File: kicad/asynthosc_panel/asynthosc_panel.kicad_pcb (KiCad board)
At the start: 2 copper layers, 71.1 x 128.4 mm, 0 parts

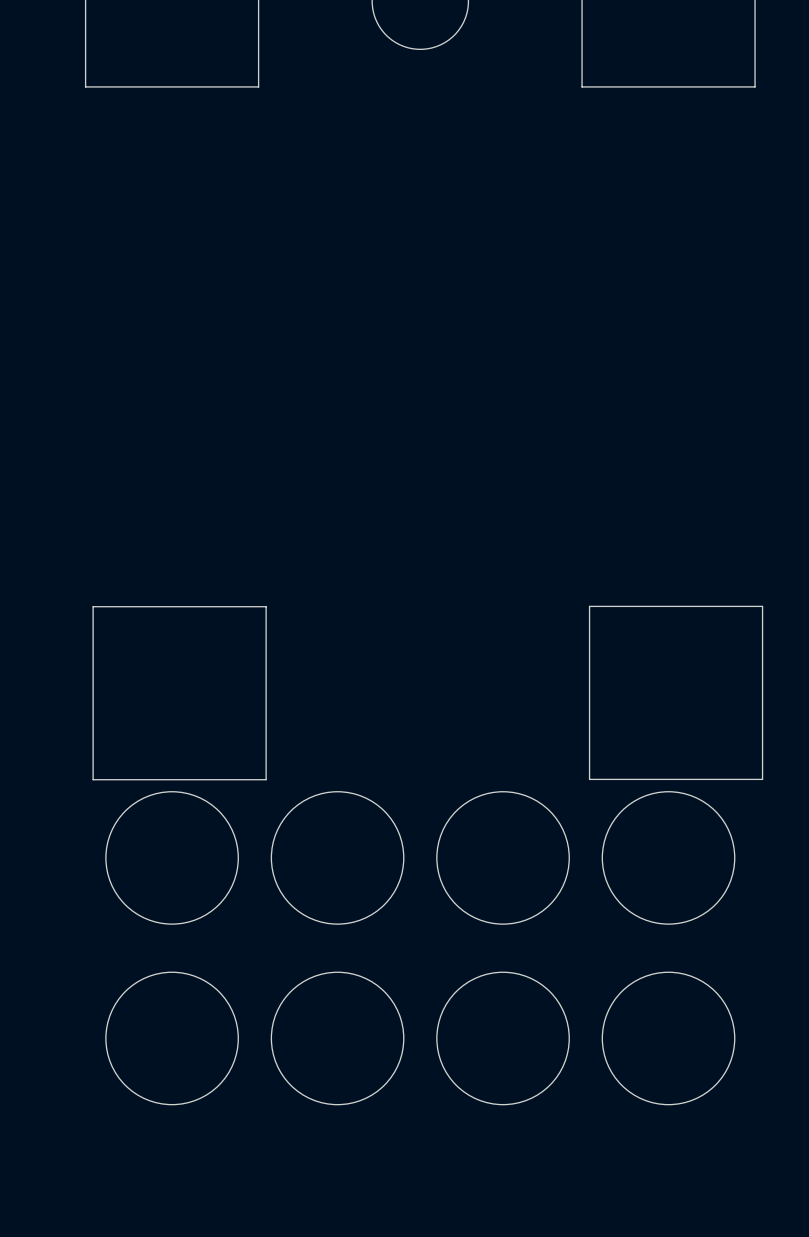
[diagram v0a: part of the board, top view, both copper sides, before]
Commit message: [MECA] Add 1mm milling contour
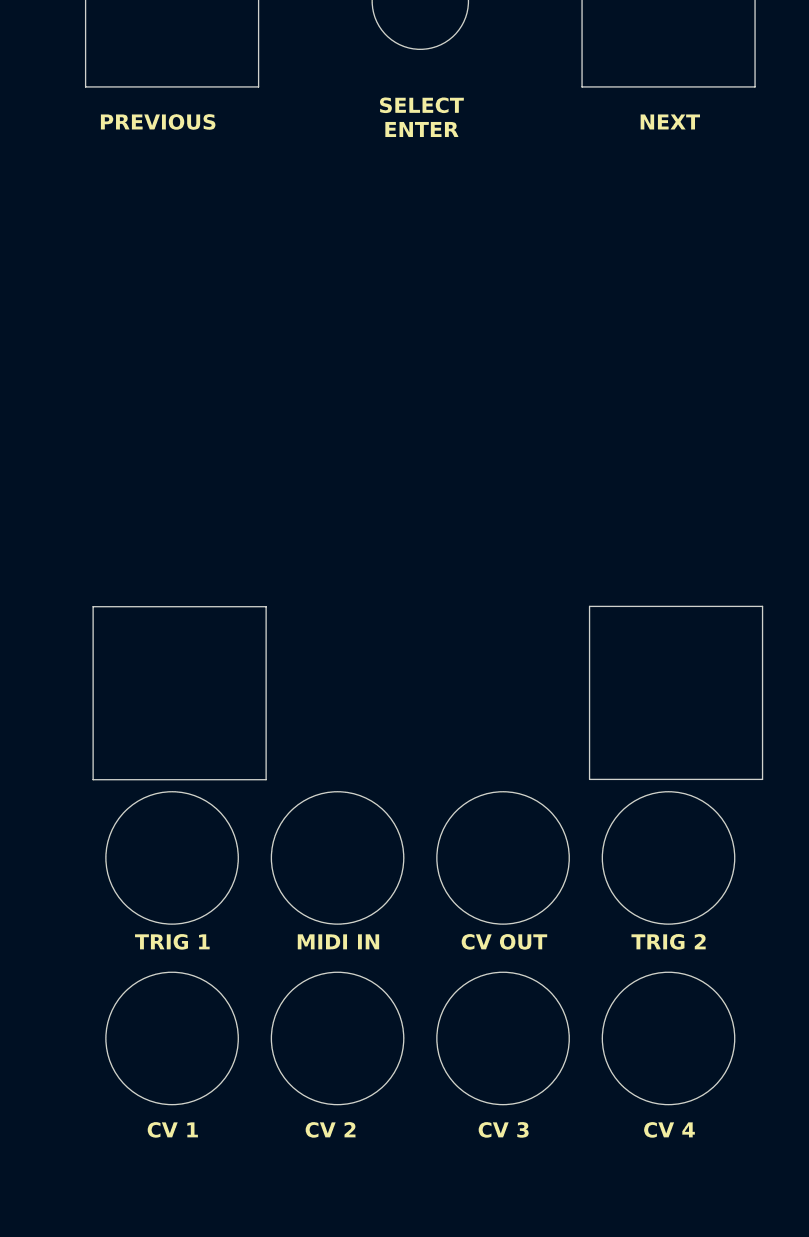
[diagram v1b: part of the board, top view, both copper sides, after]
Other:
- board text added: "CV 1"
- board text added: "CV 2"
- board text added: "CV 3"
- board text added: "CV 4"
- board text added: "CV OUT"
- board text added: "MIDI IN"
- board text added: "NEXT"
- board text added: "PREVIOUS"
- board text added: "SELECT ENTER"
- board text added: "TRIG 1"
- board text added: "TRIG 2"

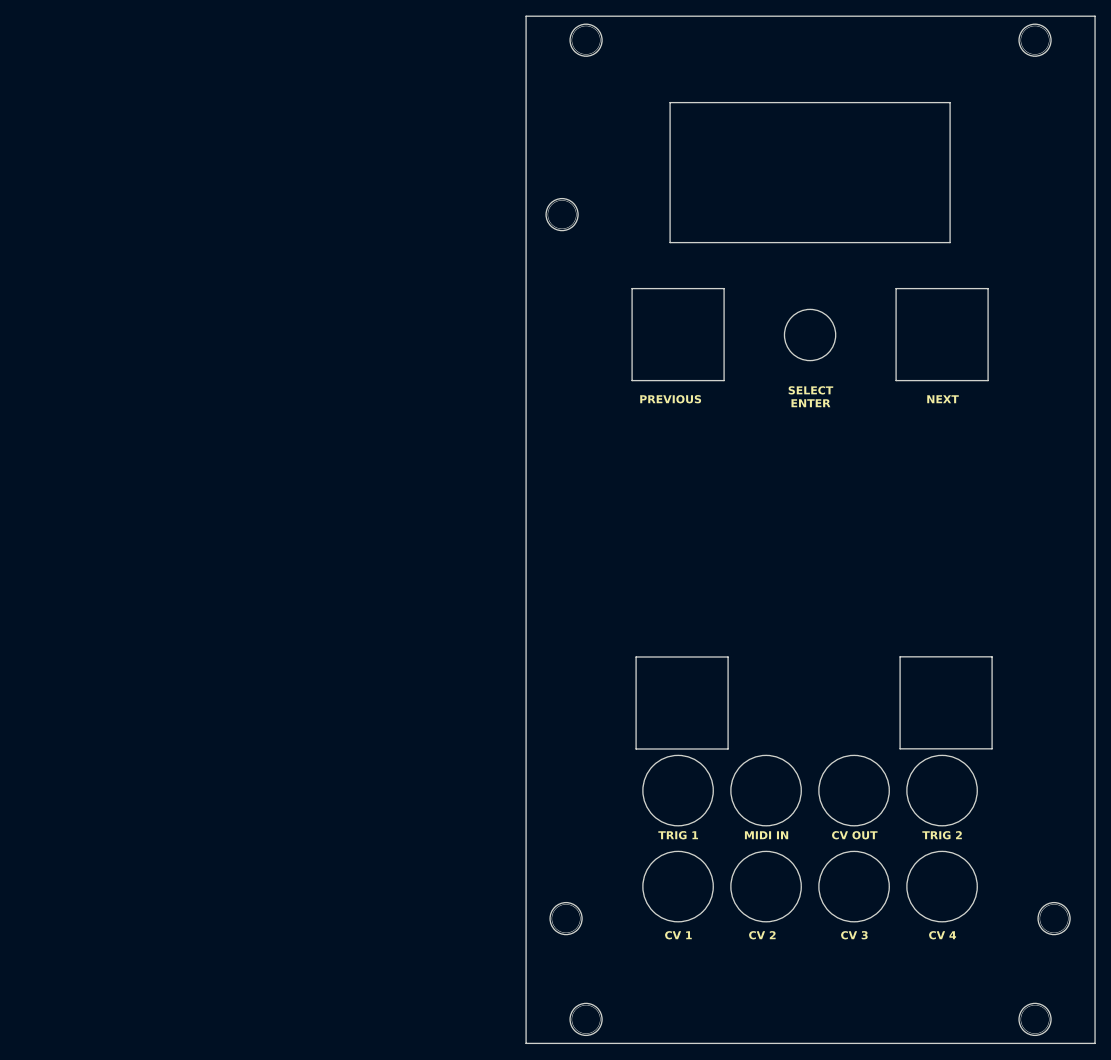
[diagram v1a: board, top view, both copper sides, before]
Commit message: [SCH][PCB] Add connector and LEDs
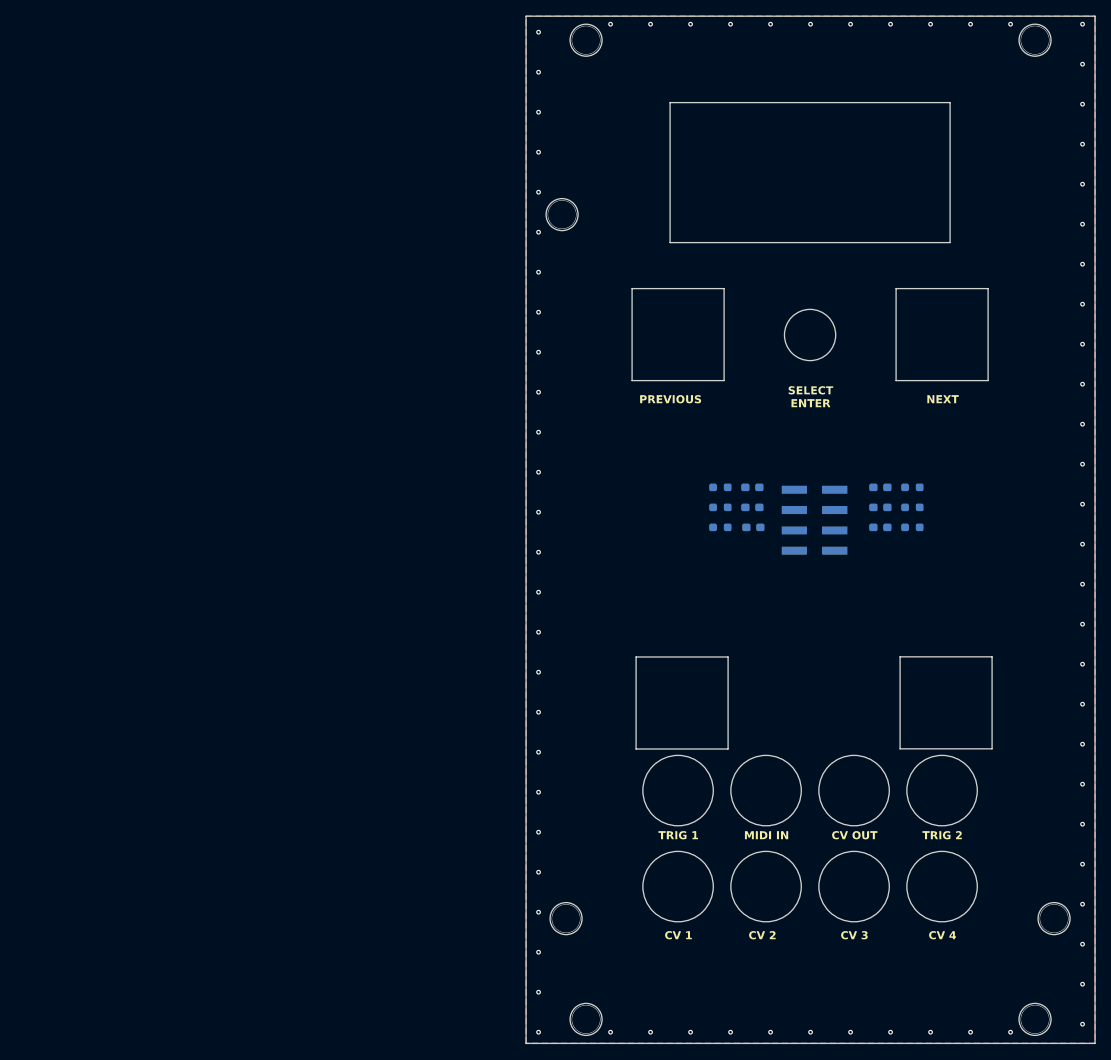
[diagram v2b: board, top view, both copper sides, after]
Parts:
- added D1: LED Red 0603, LED_SMD:LED_0603_1608Metric_Pad1.05x0.95mm_HandSolder, B.Cu at (144.3, 108.9)
- added D2: LED Red 0603, LED_SMD:LED_0603_1608Metric_Pad1.05x0.95mm_HandSolder, B.Cu at (128.3, 108.9)
- added D3: LED Red 0603, LED_SMD:LED_0603_1608Metric_Pad1.05x0.95mm_HandSolder, B.Cu at (144.3, 111.4)
- added D4: LED Red 0603, LED_SMD:LED_0603_1608Metric_Pad1.05x0.95mm_HandSolder, B.Cu at (128.3, 111.4)
- added D5: LED Red 0603, LED_SMD:LED_0603_1608Metric_Pad1.05x0.95mm_HandSolder, B.Cu at (144.3, 113.9)
- added D6: LED Red 0603, LED_SMD:LED_0603_1608Metric_Pad1.05x0.95mm_HandSolder, B.Cu at (128.4, 113.9)
- added J15: Conn_02x04_Odd_Even, Connector_PinHeader_2.54mm:PinHeader_2x04_P2.54mm_Vertical_SMD, B.Cu at (136.1, 113.0)
- added R1: 10k 0603, Resistor_SMD:R_0603_1608Metric_Pad0.98x0.95mm_HandSolder, B.Cu at (148.3, 108.9)
- added R2: 10k 0603, Resistor_SMD:R_0603_1608Metric_Pad0.98x0.95mm_HandSolder, B.Cu at (124.3, 108.9)
- added R3: 10k 0603, Resistor_SMD:R_0603_1608Metric_Pad0.98x0.95mm_HandSolder, B.Cu at (148.3, 111.4)
- added R4: 10k 0603, Resistor_SMD:R_0603_1608Metric_Pad0.98x0.95mm_HandSolder, B.Cu at (124.3, 111.4)
- added R5: 10k 0603, Resistor_SMD:R_0603_1608Metric_Pad0.98x0.95mm_HandSolder, B.Cu at (148.3, 113.9)
- added R6: 10k 0603, Resistor_SMD:R_0603_1608Metric_Pad0.98x0.95mm_HandSolder, B.Cu at (124.3, 113.9)
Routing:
- net GND: vias 0 -> 74
- added copper zone on B.Cu, net GND
- added copper zone on F.Cu, net GND

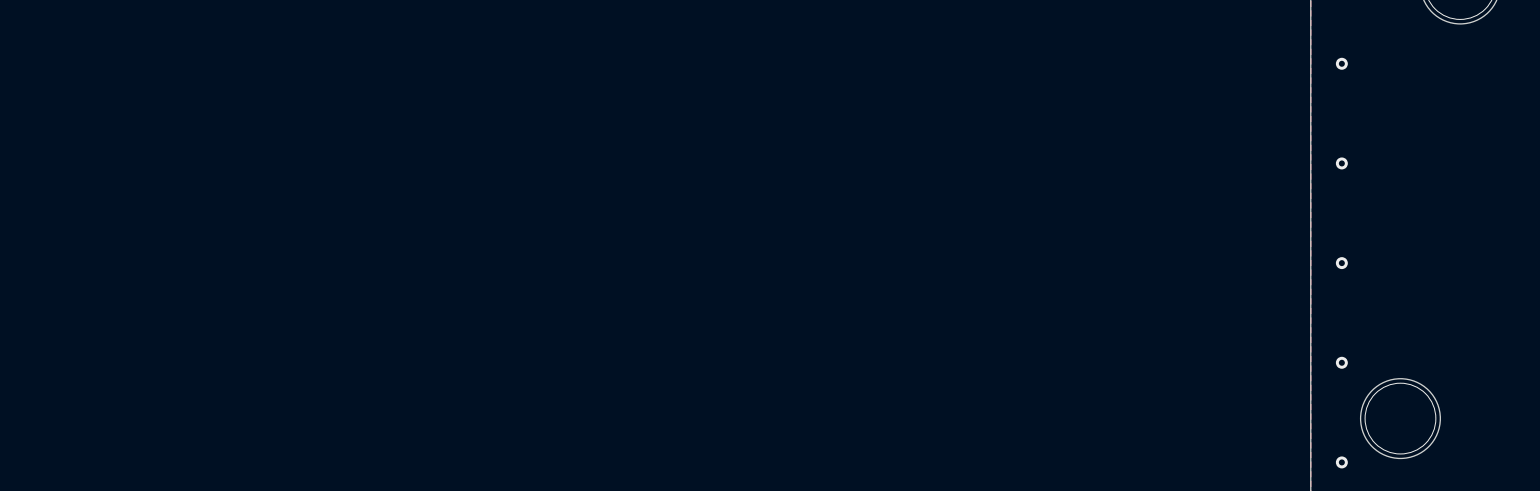
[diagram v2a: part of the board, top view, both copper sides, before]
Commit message: [PCB] Add slot for cable
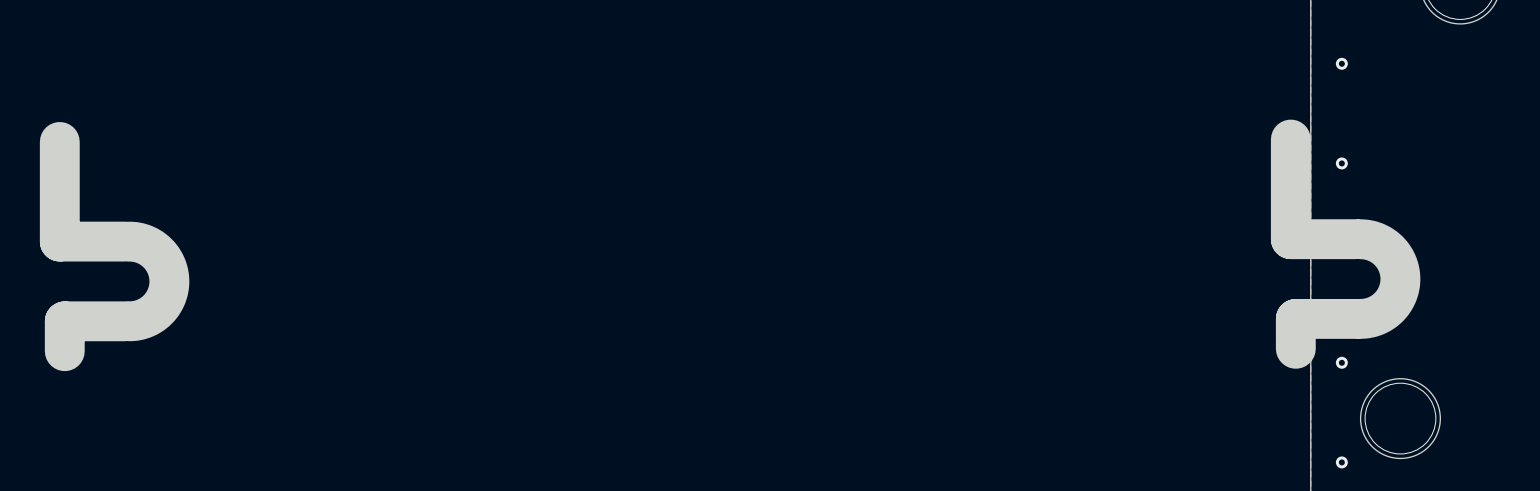
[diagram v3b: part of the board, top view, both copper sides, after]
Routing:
- net GND: vias 74 -> 73
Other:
- board size 71.1 x 128.4 mm -> 133.9 x 128.4 mm
- board text removed: "Differencial pairs (coplanar) | Width (mm) | Spacing (mm) 50 Ohms | 0.696 | 0.102 75 Ohms | 0.3 | 0.102 100 Ohms | 0.1189 | 0.11 Since 50 ohms width is too much, we use 75 ohms instead"
- board text removed: "Need 2mm at each side of USB-B connector to fit the connector body"

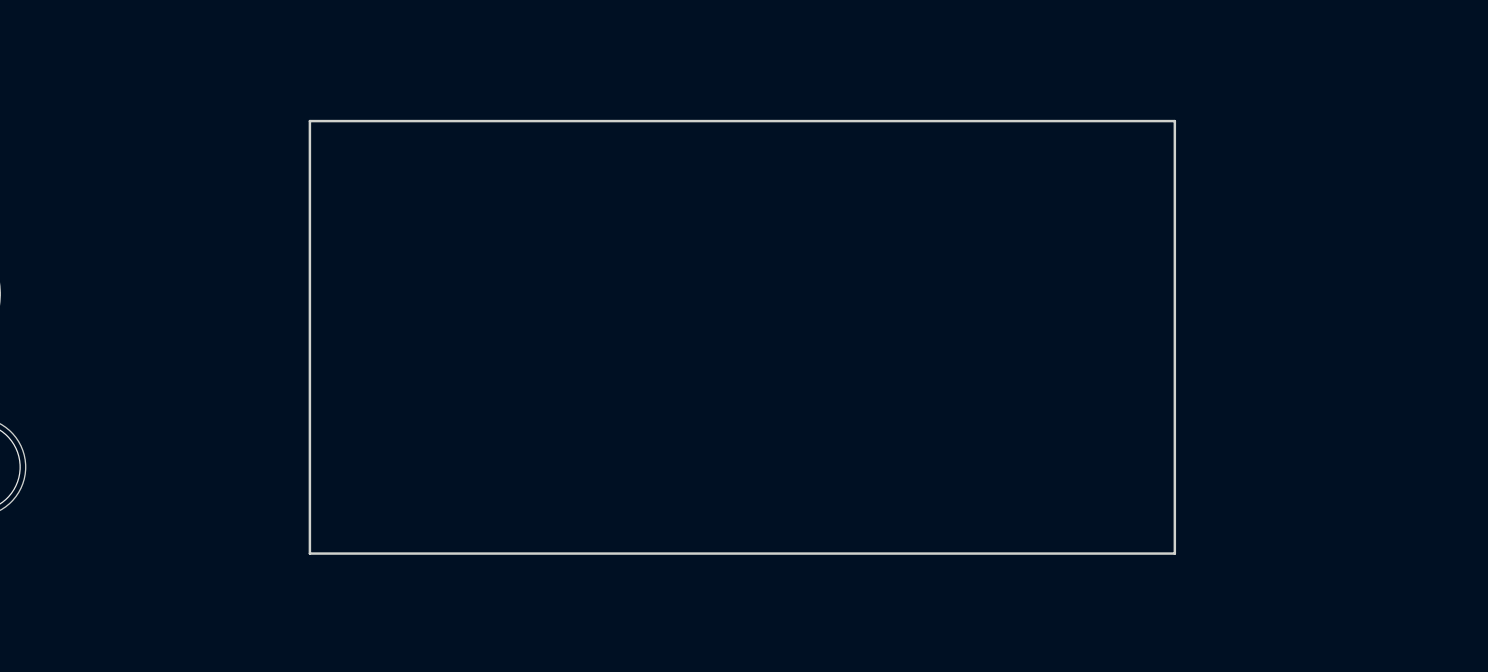
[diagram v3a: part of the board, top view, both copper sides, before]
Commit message: [PCB] Add mounting hole for display holder
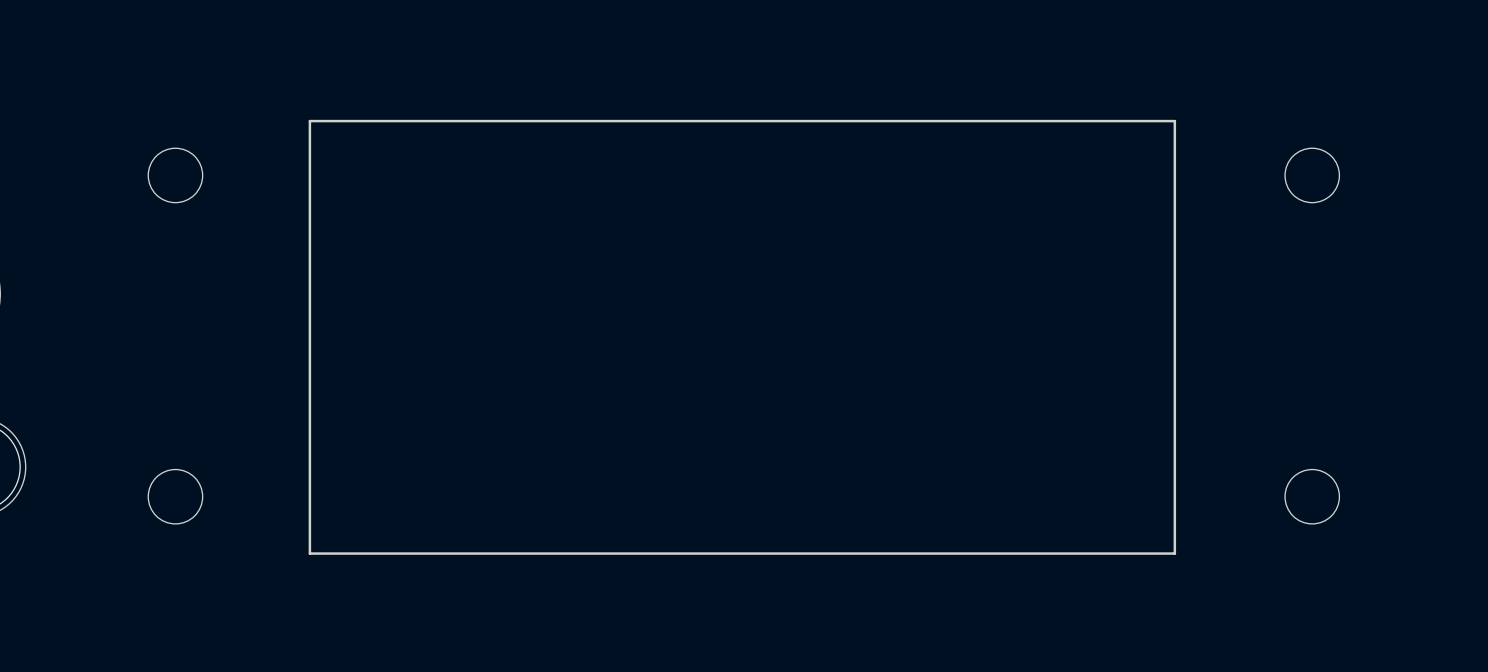
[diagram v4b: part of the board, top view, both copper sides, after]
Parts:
- added REF**: MountingHole_2.2mm_M2, MountingHole:MountingHole_2.2mm_M2, F.Cu at (158.6, 76.0)
- added REF**: MountingHole_2.2mm_M2, MountingHole:MountingHole_2.2mm_M2, F.Cu at (158.6, 63.0)
- added REF**: MountingHole_2.2mm_M2, MountingHole:MountingHole_2.2mm_M2, F.Cu at (112.6, 63.0)
- added REF**: MountingHole_2.2mm_M2, MountingHole:MountingHole_2.2mm_M2, F.Cu at (112.6, 76.0)
